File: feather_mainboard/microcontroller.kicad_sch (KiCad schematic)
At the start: 0 parts

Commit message: finished microcontroller and microsd card subsheets. TODO: button subsheets and internal connections
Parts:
- added C20, C21: 0.1µF, footprints:WCAP-CSGP_1210_H2.0, symbol WCAP-CSGP_1210_H2.0:WCAP-CSGP_1210_H2.0
- added U1: Adafruit ESP32-S3 Feather, Custom footprints:Adafruit ESP32-S3 Feather 4MB Flash 2MB PSRAM, symbol Adafruit ESP32-S3 Feather 4MB Flash 2MB PSRAM:Adafruit_ESP32-S3_Feather
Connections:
- new net 3V3: C20.1, C21.1, U1.2 (3V3), U1.3 (3V3)
- new net Button3: U1.14 (RX)
- new net Button4: U1.15 (TX)
- new net Button_1: U1.6 (A1)
- new net Button_2: U1.7 (A2)
- new net DISPLAY_BUSY: U1.10 (A5)
- new net DISPLAY_DC: U1.8 (A3)
- new net DISPLAY_RST: U1.9 (A4)
- new net Display-Enable: U1.5 (A0)
- new net GND: C20.2, C21.2, U1.4 (GND)
- new net IIC_SCL: U1.27 (SCL)
- new net IIC_SDA: U1.28 (SDA)
- new net Reset: U1.1 (Reset)
- new net SD_CD: U1.26 (D5)
- new net SD_DAT1: U1.25 (D6)
- new net SD_DAT2: U1.24 (D9)
- new net SPI_1_MISO: U1.13 (MISO)
- new net SPI_1_MOSI: U1.12 (MOSI)
- new net SPI_1_SCK: U1.11 (SCK)
- new net SPI_2_CS: U1.23 (D10)
- new net SPI_2_MISO: U1.20 (D13)
- new net SPI_2_MOSI: U1.22 (D11)
- new net SPI_2_SCK: U1.21 (D12)
- no-connect marks 0 -> 4

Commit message: schematic is almost done (check TODOs in schematic file)
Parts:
- renumbered C20 to C1, C21 to C2
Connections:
- net Button3 is gone; now on net Button_2: U1.14 (RX)
- net Button_1: now also U1.7 (A2); no longer U1.6 (A1)
- net Button_2: no longer U1.7 (A2)
- net Button4 renamed Button_3
- net SPI_1_MISO renamed DISPLAY_CS
- net SPI_1_MOSI renamed DISPLAY_MOSI
- net SPI_1_SCK renamed DISPLAY_SCLK
- net SPI_2_CS renamed SD_CS/DAT3
- net SPI_2_MISO renamed SD_MISO/CMD
- net SPI_2_MOSI renamed SD_MOSI/DAT0
- net SPI_2_SCK renamed SD_CLK
- new net Free: U1.6 (A1)
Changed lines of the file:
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@@
 		)
 	)
-	(hierarchical_label "SPI_2_MISO"
+	(hierarchical_label "SD_MISO{slash}CMD"
 		(shape bidirectional)
 		(at 222.25 93.98 0)
@@
 		)
 	)
-	(hierarchical_label "SPI_2_CS"
+	(hierarchical_label "SD_CS{slash}DAT3"
 		(shape bidirectional)
 		(at 222.25 105.41 0)
@@
 		)
 	)
-	(hierarchical_label "SPI_1_MISO"
+	(hierarchical_label "DISPLAY_CS"
 		(shape bidirectional)
 		(at 95.25 113.03 180)
@@
 		)
 	)
-	(hierarchical_label "SPI_2_MOSI"
+	(hierarchical_label "SD_MOSI{slash}DAT0"
 		(shape bidirectional)
 		(at 222.25 101.6 0)
@@
 		)
 	)
-	(hierarchical_label "SPI_2_SCK"
+	(hierarchical_label "SD_CLK"
 		(shape bidirectional)
 		(at 222.25 97.79 0)
@@
 		)
 	)
-	(hierarchical_label "Button3"
+	(hierarchical_label "Button_2"
 		(shape bidirectional)
 		(at 95.25 116.84 180)
@@
 		)
 	)
-	(hierarchical_label "Button_2"
+	(hierarchical_label "Button_1"
 		(shape bidirectional)
 		(at 95.25 90.17 180)
@@
 		)
 	)
-	(hierarchical_label "Button4"
+	(hierarchical_label "Button_3"
 		(shape bidirectional)
 		(at 95.25 120.65 180)
@@
 		)
 	)
-	(hierarchical_label "Button_1"
+	(hierarchical_label "Free"
 		(shape bidirectional)
 		(at 95.25 86.36 180)
@@
 		)
 	)
-	(hierarchical_label "SPI_1_MOSI"
+	(hierarchical_label "DISPLAY_MOSI"
 		(shape bidirectional)
 		(at 95.25 109.22 180)
@@
 		)
 	)
-	(hierarchical_label "SPI_1_SCK"
+	(hierarchical_label "DISPLAY_SCLK"
 		(shape bidirectional)
 		(at 95.25 105.41 180)
@@
 		(on_board yes)
 		(dnp no)
-		(property "Reference" "C20"
+		(property "Reference" "C1"
 			(at 131.572 50.8 0)
 			(effects
@@
 			(project "feather_mainboard"
 				(path "/e1e12730-ab4f-45db-8b66-c1e0f78e2f00/2e3e5636-c492-45ef-bece-a2815296f467"
-					(reference "C20")
+					(reference "C1")
 					(unit 1)
 				)
@@
 		(on_board yes)
 		(dnp no)
-		(property "Reference" "C21"
+		(property "Reference" "C2"
 			(at 116.078 50.8 0)
 			(effects
@@
 			(project "feather_mainboard"
 				(path "/e1e12730-ab4f-45db-8b66-c1e0f78e2f00/2e3e5636-c492-45ef-bece-a2815296f467"
-					(reference "C21")
+					(reference "C2")
 					(unit 1)
 				)

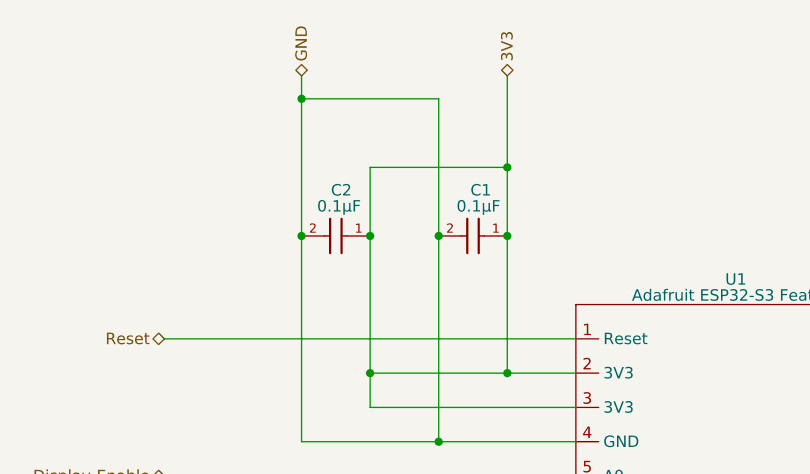
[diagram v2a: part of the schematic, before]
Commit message: changed footprints location to match the new folder. TODO: check if the path is working on another computer
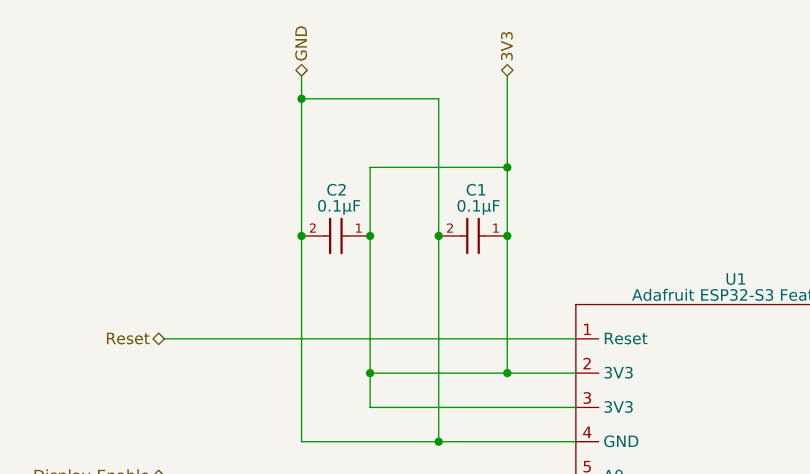
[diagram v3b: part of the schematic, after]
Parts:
- C1, C2: footprint footprints:WCAP-CSGP_1210_H2.0 -> Custom footprints:WCAP-CSGP_1210_H2.0
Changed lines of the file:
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@@
 	)
 	(symbol
+		(lib_name "WCAP-CSGP_1210_H2.0_1")
 		(lib_id "WCAP-CSGP_1210_H2.0:WCAP-CSGP_1210_H2.0")
 		(at 130.81 55.88 180)
@@
 		(dnp no)
 		(property "Reference" "C1"
-			(at 131.572 50.8 0)
+			(at 131.064 50.8 0)
 			(effects
 				(font
@@
 			)
 		)
-		(property "Footprint" "footprints:WCAP-CSGP_1210_H2.0"
+		(property "Footprint" "Custom footprints:WCAP-CSGP_1210_H2.0"
 			(at 130.81 55.88 0)
 			(effects
@@
 		(dnp no)
 		(property "Reference" "C2"
-			(at 116.078 50.8 0)
+			(at 115.57 50.8 0)
 			(effects
 				(font
@@
 			)
 		)
-		(property "Footprint" "footprints:WCAP-CSGP_1210_H2.0"
+		(property "Footprint" "Custom footprints:WCAP-CSGP_1210_H2.0"
 			(at 115.57 55.88 0)
 			(effects

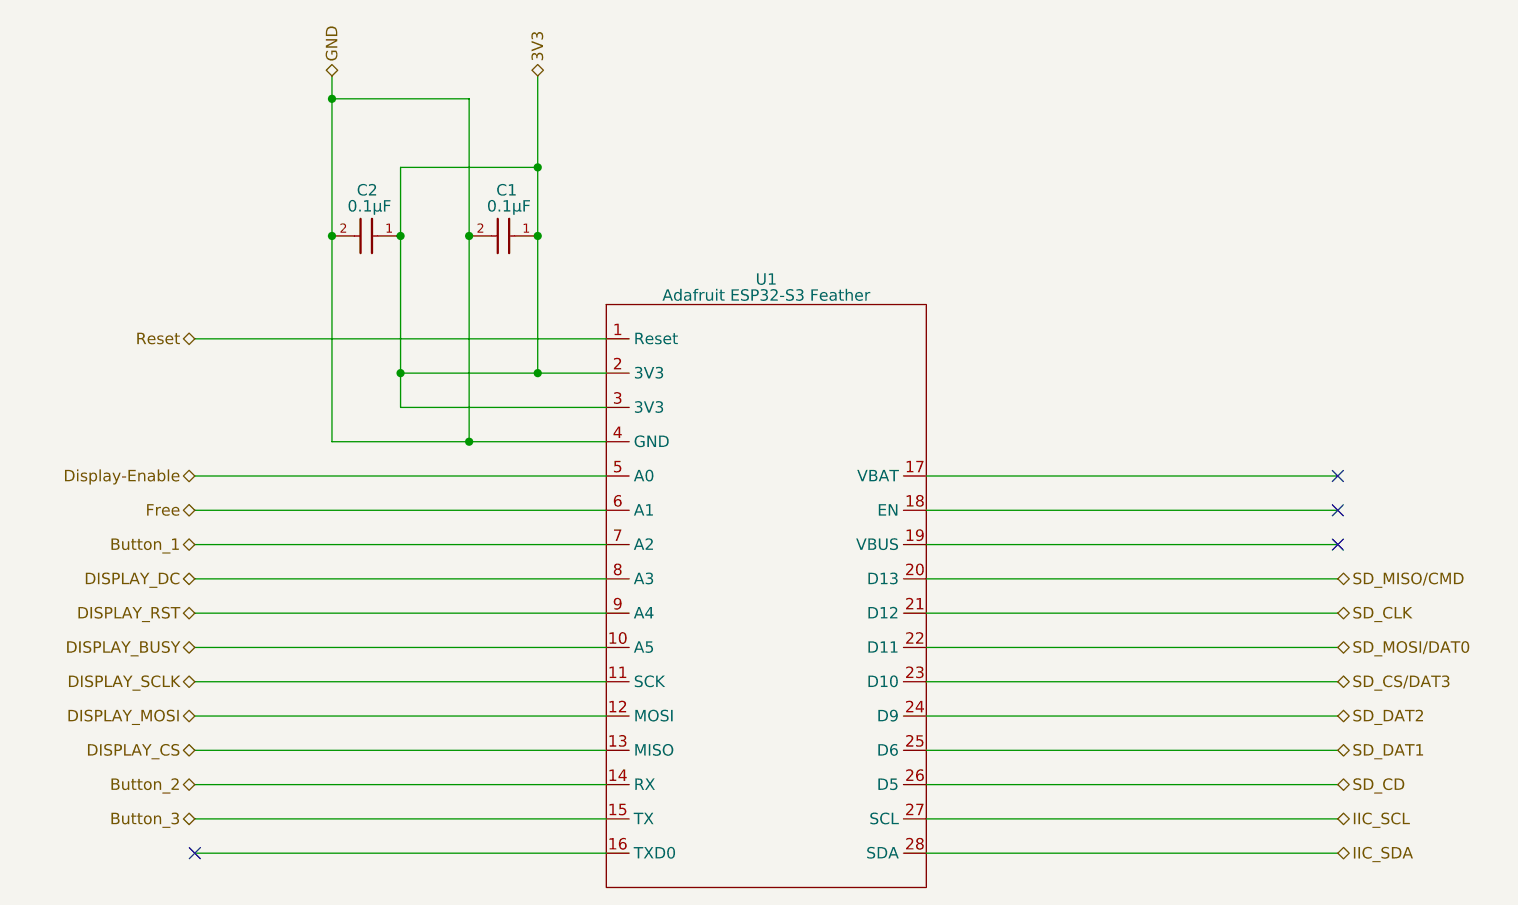
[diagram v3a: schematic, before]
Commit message: added daughter board
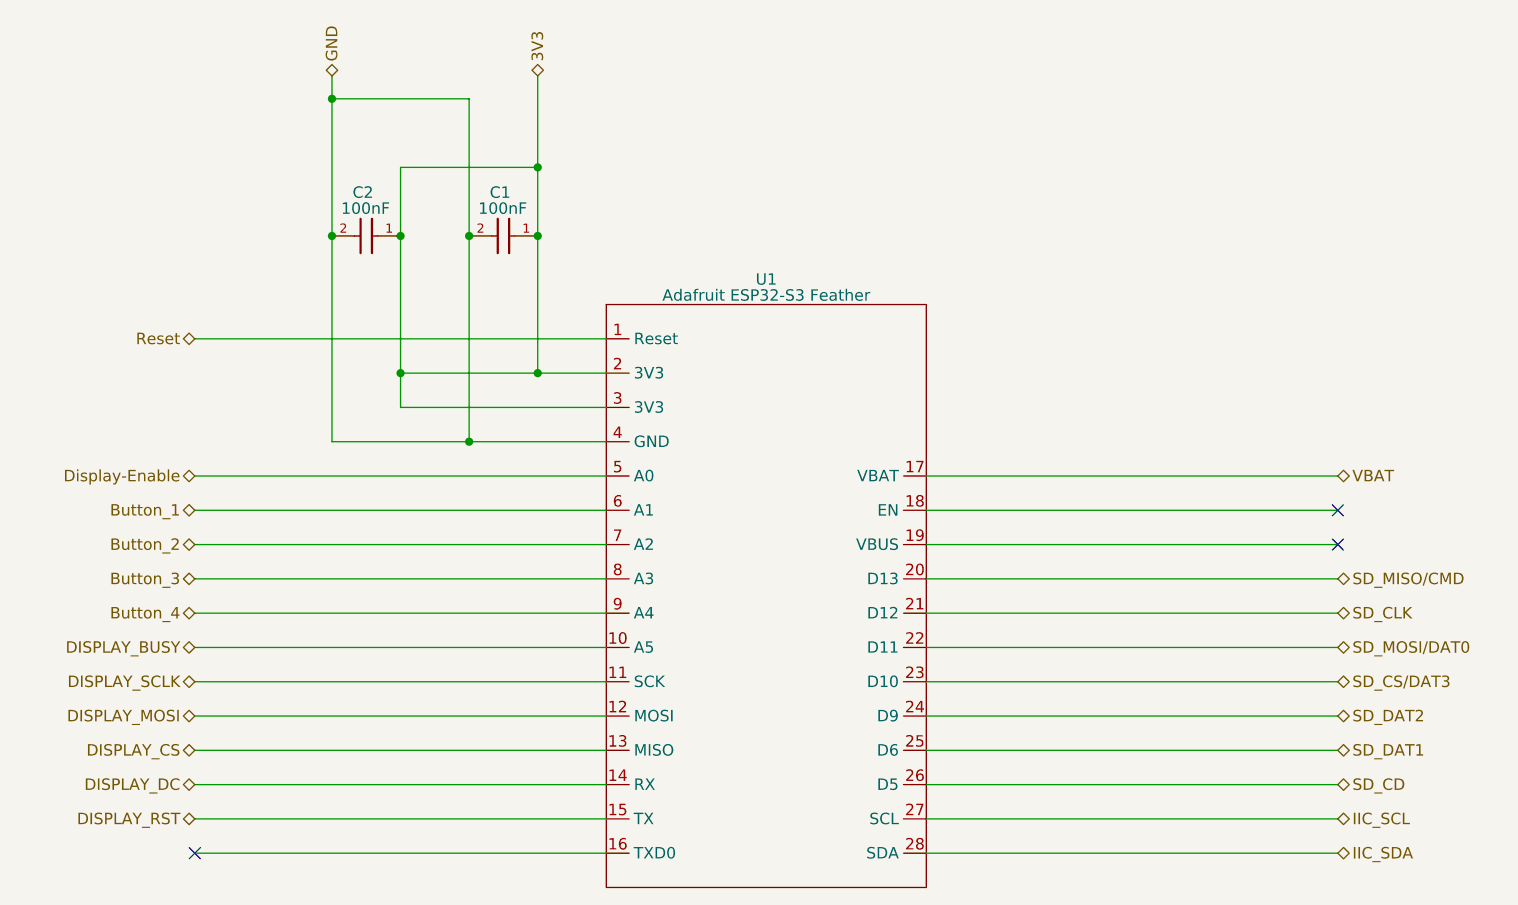
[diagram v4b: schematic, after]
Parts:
- removed C1, C2: 0.1µF, Custom footprints:WCAP-CSGP_1210_H2.0, symbol WCAP-CSGP_1210_H2.0:WCAP-CSGP_1210_H2.0
- added C1, C2: 100nF, Custom footprints:WCAP-CSGP_0603_R, symbol WCAP-CSGP_0603:WCAP-CSGP_0603
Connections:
- net Free is gone; now on net Button_1: U1.6 (A1)
- net 3V3: now also C1.1, C2.1
- net Button_1: no longer U1.7 (A2)
- net Button_2: now also U1.7 (A2); no longer U1.14 (RX)
- net Button_3: now also U1.8 (A3); no longer U1.15 (TX)
- net DISPLAY_DC: now also U1.14 (RX); no longer U1.8 (A3)
- net DISPLAY_RST: now also U1.15 (TX); no longer U1.9 (A4)
- net GND: now also C1.2, C2.2
- net VBAT: now reaches U1.17 (VBAT)
- new net Button_4: U1.9 (A4)
- no-connect marks 4 -> 3

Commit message: finished mainboard design, need to do the routing
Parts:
- renumbered C1 to C1_1, C2 to C1_2
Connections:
- net VBAT: no longer names the net of U1.17 (VBAT)
- no-connect marks 3 -> 4
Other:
- moved on the sheet: U1
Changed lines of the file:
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@@
+	)
+	(no_connect
+		(at 222.25 82.55)
 	)
 	(no_connect
@@
 	(wire
 		(pts
+			(xy 177.8 113.03) (xy 222.25 113.03)
+		)
+		(stroke
+			(width 0)
+			(type default)
+		)
+	)
+	(wire
+		(pts
 			(xy 110.49 78.74) (xy 125.73 78.74)
 		)
@@
 	(wire
 		(pts
+			(xy 177.8 97.79) (xy 222.25 97.79)
+		)
+		(stroke
+			(width 0)
+			(type default)
+		)
+	)
+	(wire
+		(pts
 			(xy 95.25 124.46) (xy 140.97 124.46)
 		)
@@
 	(wire
 		(pts
+			(xy 177.8 120.65) (xy 222.25 120.65)
+		)
+		(stroke
+			(width 0)
+			(type default)
+		)
+	)
+	(wire
+		(pts
 			(xy 95.25 109.22) (xy 140.97 109.22)
 		)
@@
 	(wire
 		(pts
-			(xy 176.53 90.17) (xy 222.25 90.17)
-		)
-		(stroke
-			(width 0)
-			(type default)
-		)
-	)
-	(wire
-		(pts
 			(xy 95.25 67.31) (xy 140.97 67.31)
 		)
@@
 	(wire
 		(pts
+			(xy 177.8 116.84) (xy 222.25 116.84)
+		)
+		(stroke
+			(width 0)
+			(type default)
+		)
+	)
+	(wire
+		(pts
+			(xy 177.8 101.6) (xy 222.25 101.6)
+		)
+		(stroke
+			(width 0)
+			(type default)
+		)
+	)
+	(wire
+		(pts
 			(xy 95.25 90.17) (xy 140.97 90.17)
 		)
@@
 	(wire
 		(pts
-			(xy 176.53 97.79) (xy 222.25 97.79)
-		)
-		(stroke
-			(width 0)
-			(type default)
-		)
-	)
-	(wire
-		(pts
 			(xy 118.11 71.12) (xy 118.11 74.93)
 		)
@@
 	(wire
 		(pts
+			(xy 177.8 86.36) (xy 222.25 86.36)
+		)
+		(stroke
+			(width 0)
+			(type default)
+		)
+	)
+	(wire
+		(pts
 			(xy 95.25 116.84) (xy 140.97 116.84)
 		)
@@
 	(wire
 		(pts
-			(xy 176.53 105.41) (xy 222.25 105.41)
+			(xy 177.8 109.22) (xy 222.25 109.22)
 		)
 		(stroke
@@
 	(wire
 		(pts
-			(xy 176.53 82.55) (xy 222.25 82.55)
-		)
-		(stroke
-			(width 0)
-			(type default)
-		)
-	)
-	(wire
-		(pts
 			(xy 95.25 101.6) (xy 140.97 101.6)
 		)
@@
 	(wire
 		(pts
-			(xy 176.53 109.22) (xy 222.25 109.22)
-		)
-		(stroke
-			(width 0)
-			(type default)
-		)
-	)
-	(wire
-		(pts
-			(xy 176.53 93.98) (xy 222.25 93.98)
+			(xy 177.8 105.41) (xy 222.25 105.41)
+		)
+		(stroke
+			(width 0)
+			(type default)
+		)
+	)
+	(wire
+		(pts
+			(xy 177.8 124.46) (xy 222.25 124.46)
 		)
 		(stroke
@@
 	(wire
 		(pts
-			(xy 176.53 101.6) (xy 222.25 101.6)
-		)
-		(stroke
-			(width 0)
-			(type default)
-		)
-	)
-	(wire
-		(pts
 			(xy 125.73 78.74) (xy 140.97 78.74)
 		)
@@
 	(wire
 		(pts
-			(xy 176.53 86.36) (xy 222.25 86.36)
-		)
-		(stroke
-			(width 0)
-			(type default)
-		)
-	)
-	(wire
-		(pts
-			(xy 176.53 120.65) (xy 222.25 120.65)
-		)
-		(stroke
-			(width 0)
-			(type default)
-		)
-	)
-	(wire
-		(pts
-			(xy 176.53 116.84) (xy 222.25 116.84)
-		)
-		(stroke
-			(width 0)
-			(type default)
-		)
-	)
-	(wire
-		(pts
 			(xy 118.11 48.26) (xy 118.11 55.88)
 		)
@@
 	(wire
 		(pts
-			(xy 176.53 113.03) (xy 222.25 113.03)
+			(xy 177.8 90.17) (xy 222.25 90.17)
 		)
 		(stroke
@@
 	(wire
 		(pts
+			(xy 177.8 93.98) (xy 222.25 93.98)
+		)
+		(stroke
+			(width 0)
+			(type default)
+		)
+	)
+	(wire
+		(pts
 			(xy 95.25 120.65) (xy 140.97 120.65)
 		)
@@
 	(wire
 		(pts
+			(xy 177.8 82.55) (xy 222.25 82.55)
+		)
+		(stroke
+			(width 0)
+			(type default)
+		)
+	)
+	(wire
+		(pts
 			(xy 133.35 71.12) (xy 140.97 71.12)
 		)
@@
 		)
 	)
-	(wire
-		(pts
-			(xy 176.53 124.46) (xy 222.25 124.46)
-		)
-		(stroke
-			(width 0)
-			(type default)
-		)
-	)
 	(hierarchical_label "Display-Enable"
 		(shape bidirectional)
@@
 			)
 			(justify right)
-		)
-	)
-	(hierarchical_label "VBAT"
-		(shape bidirectional)
-		(at 222.25 82.55 0)
-		(fields_autoplaced yes)
-		(effects
-			(font
-				(size 1.27 1.27)
-			)
-			(justify left)
 		)
 	)
@@
 	(symbol
 		(lib_id "Adafruit ESP32-S3 Feather 4MB Flash 2MB PSRAM:Adafruit_ESP32-S3_Feather")
-		(at 158.75 95.25 0)
+		(at 158.75 93.98 0)
 		(unit 1)
 		(exclude_from_sim no)
@@
 		(fields_autoplaced yes)
 		(property "Reference" "U1"
-			(at 158.75 60.706 0)
+			(at 158.75 59.436 0)
 			(effects
 				(font
@@
 		)
 		(property "Value" "Adafruit ESP32-S3 Feather"
-			(at 158.75 62.484 0)
+			(at 158.75 61.214 0)
 			(effects
 				(font
@@
 		)
 		(property "Footprint" "Custom footprints:Adafruit ESP32-S3 Feather 4MB Flash 2MB PSRAM"
-			(at 158.75 129.54 0)
+			(at 158.75 128.27 0)
 			(effects
 				(font
@@
 		)
 		(property "Datasheet" ""
-			(at 153.67 101.6 0)
+			(at 153.67 100.33 0)
 			(effects
 				(font
@@
 		)
 		(property "Description" ""
-			(at 153.67 101.6 0)
+			(at 153.67 100.33 0)
 			(effects
 				(font
@@
 		(on_board yes)
 		(dnp no)
-		(property "Reference" "C2"
-			(at 112.776 51.054 0)
+		(property "Reference" "C1_2"
+			(at 111.76 51.054 0)
 			(effects
 				(font
@@
 		)
 		(property "Value" "100nF"
-			(at 111.506 52.832 0)
+			(at 111.252 52.832 0)
 			(effects
 				(font
@@
 			(project "feather_mainboard"
 				(path "/e1e12730-ab4f-45db-8b66-c1e0f78e2f00/2e3e5636-c492-45ef-bece-a2815296f467"
-					(reference "C2")
+					(reference "C1_2")
 					(unit 1)
 				)
@@
 		(on_board yes)
 		(dnp no)
-		(property "Reference" "C1"
-			(at 128.016 51.054 0)
+		(property "Reference" "C1_1"
+			(at 127.254 51.054 0)
 			(effects
 				(font
@@
 			(project "feather_mainboard"
 				(path "/e1e12730-ab4f-45db-8b66-c1e0f78e2f00/2e3e5636-c492-45ef-bece-a2815296f467"
-					(reference "C1")
+					(reference "C1_1")
 					(unit 1)
 				)

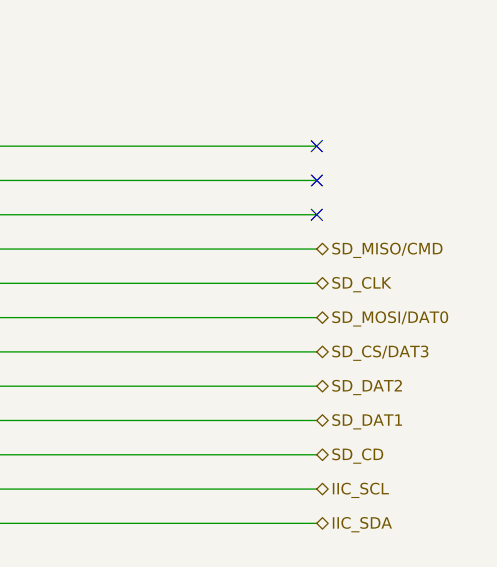
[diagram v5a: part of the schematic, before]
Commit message: Corrected/switched the names of MISO and MOSI pins
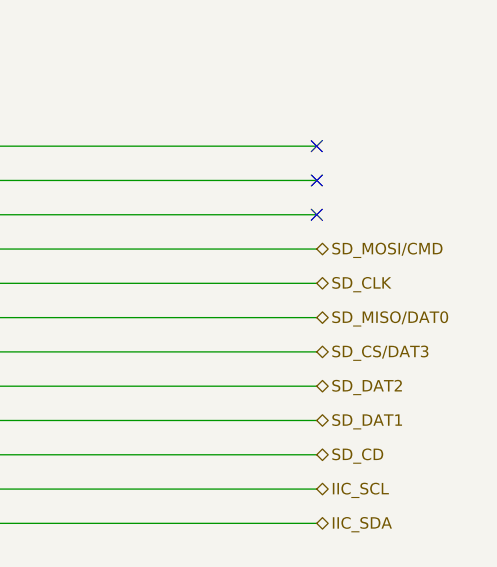
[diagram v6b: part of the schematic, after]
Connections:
- net SD_MISO/CMD renamed SD_MOSI/CMD
- net SD_MOSI/DAT0 renamed SD_MISO/DAT0
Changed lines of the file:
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@@
 		)
 	)
-	(hierarchical_label "SD_MISO{slash}CMD"
+	(hierarchical_label "SD_MOSI{slash}CMD"
 		(shape bidirectional)
 		(at 222.25 93.98 0)
@@
 		)
 	)
-	(hierarchical_label "SD_MOSI{slash}DAT0"
+	(hierarchical_label "SD_MISO{slash}DAT0"
 		(shape bidirectional)
 		(at 222.25 101.6 0)
